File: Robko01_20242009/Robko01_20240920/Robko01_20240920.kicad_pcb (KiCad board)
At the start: 2 copper layers, 178.8 x 143.8 mm, 72 parts, among them J1 Conn_01x04_Pin, J10 Motors, J11 Motors, J12 Conn_01x04_Pin, J13 Conn_01x02_Pin, J14 Conn_01x04_Pin, J15 Conn_01x02_Pin, J16 Conn_01x04_Pin, J17 Conn_01x02_Male, J18 Conn_01x02_Male, J2 Conn_01x02_Pin, J20 Conn_01x02_Male, J21 Conn_01x19_Pin, J22 Conn_01x19_Pin, J23 Conn_01x06_Pin, J24 Conn_01x04_Pin, J25 Conn_01x04_Pin, J26 Conn_01x04_Pin, J27 Conn_01x06_Pin, J28 Conn_01x02_Male, J29 Conn_01x07_Pin, J3 Conn_01x02_Pin, J30 Conn_01x02_Male, J4 Conn_01x04_Pin, J5 Conn_01x02_Pin, J6 Conn_01x04_Pin, J7 Conn_01x02_Male, J8 Conn_01x02_Pin, J9 Motors, K2 G5V-2, SW1 SW_DIP_x04, SW2 SW_DIP_x04, SW3 SW_DIP_x04, SW4 SW_DIP_x04, SW5 SW_DIP_x04, SW7 SW_DIP_x04, U1 LM7805_TO220

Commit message: Add reset button and E-Stop
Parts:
- removed R3: 15k, Resistor_THT:R_Axial_DIN0207_L6.3mm_D2.5mm_P10.16mm_Horizontal
- added J19: Conn_01x02_Male, Connector_PinHeader_2.54mm:PinHeader_1x02_P2.54mm_Vertical, F.Cu at (84.7, 87.9)
- added U2: PC817, Package_DIP:DIP-4_W7.62mm, F.Cu at (127.3, 27.5)
- J20: footprint Connector_PinHeader_2.54mm:PinHeader_1x02_P2.54mm_Vertical -> Connector_PinHeader_2.54mm:PinHeader_1x02_P2.54mm_Horizontal
- R2: value 51k -> 2k
- moved J20 53.5 mm to (101.9, 32.5), turned to -90 degrees
- moved R2 6.05 mm to (139.8, 24.0)
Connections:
- J17 pad 2: unconnected-(J17-Pin_2-Pad2) -> MC_POWER
- J18 pad 1: Net-(J18-Pin_1) -> GND
- J18 pad 2: GND -> Net-(J18-Pin_2)
- J20 pad 2: GND -> MCU_RESET
- J21 pad 2: unconnected-(J21-Pin_2-Pad2) -> MCU_RESET
- R2 pad 2: Net-(J18-Pin_1) -> Net-(R2-Pad2)
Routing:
- net MCU_RESET: track 0.00 -> 69.1 mm, vias 0 -> 2
- net Net-(J18-Pin_1): track 13.7 -> 0.00 mm
- net Net-(J18-Pin_2): track 0.00 -> 7.32 mm
- net MC_POWER: track 310.2 -> 303.8 mm
- net Net-(R2-Pad2): track 0.00 -> 5.60 mm
- net GND: vias 179 -> 178

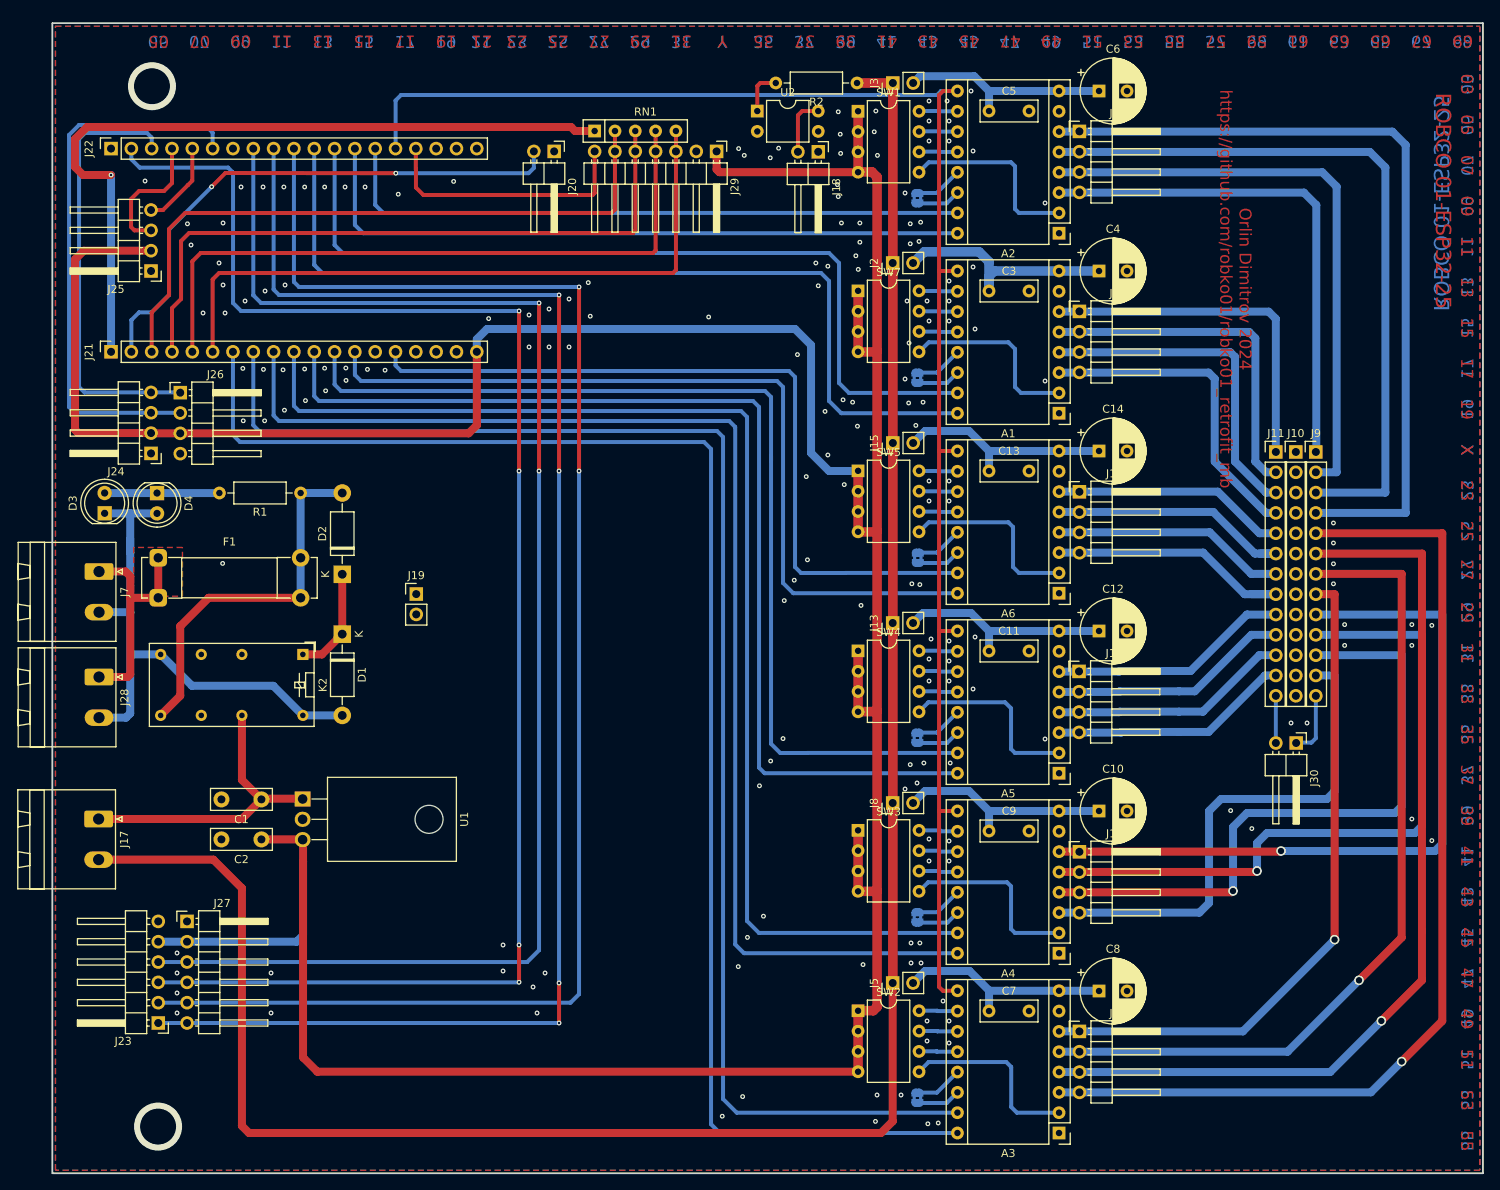
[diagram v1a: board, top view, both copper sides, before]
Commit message: Add UEXT
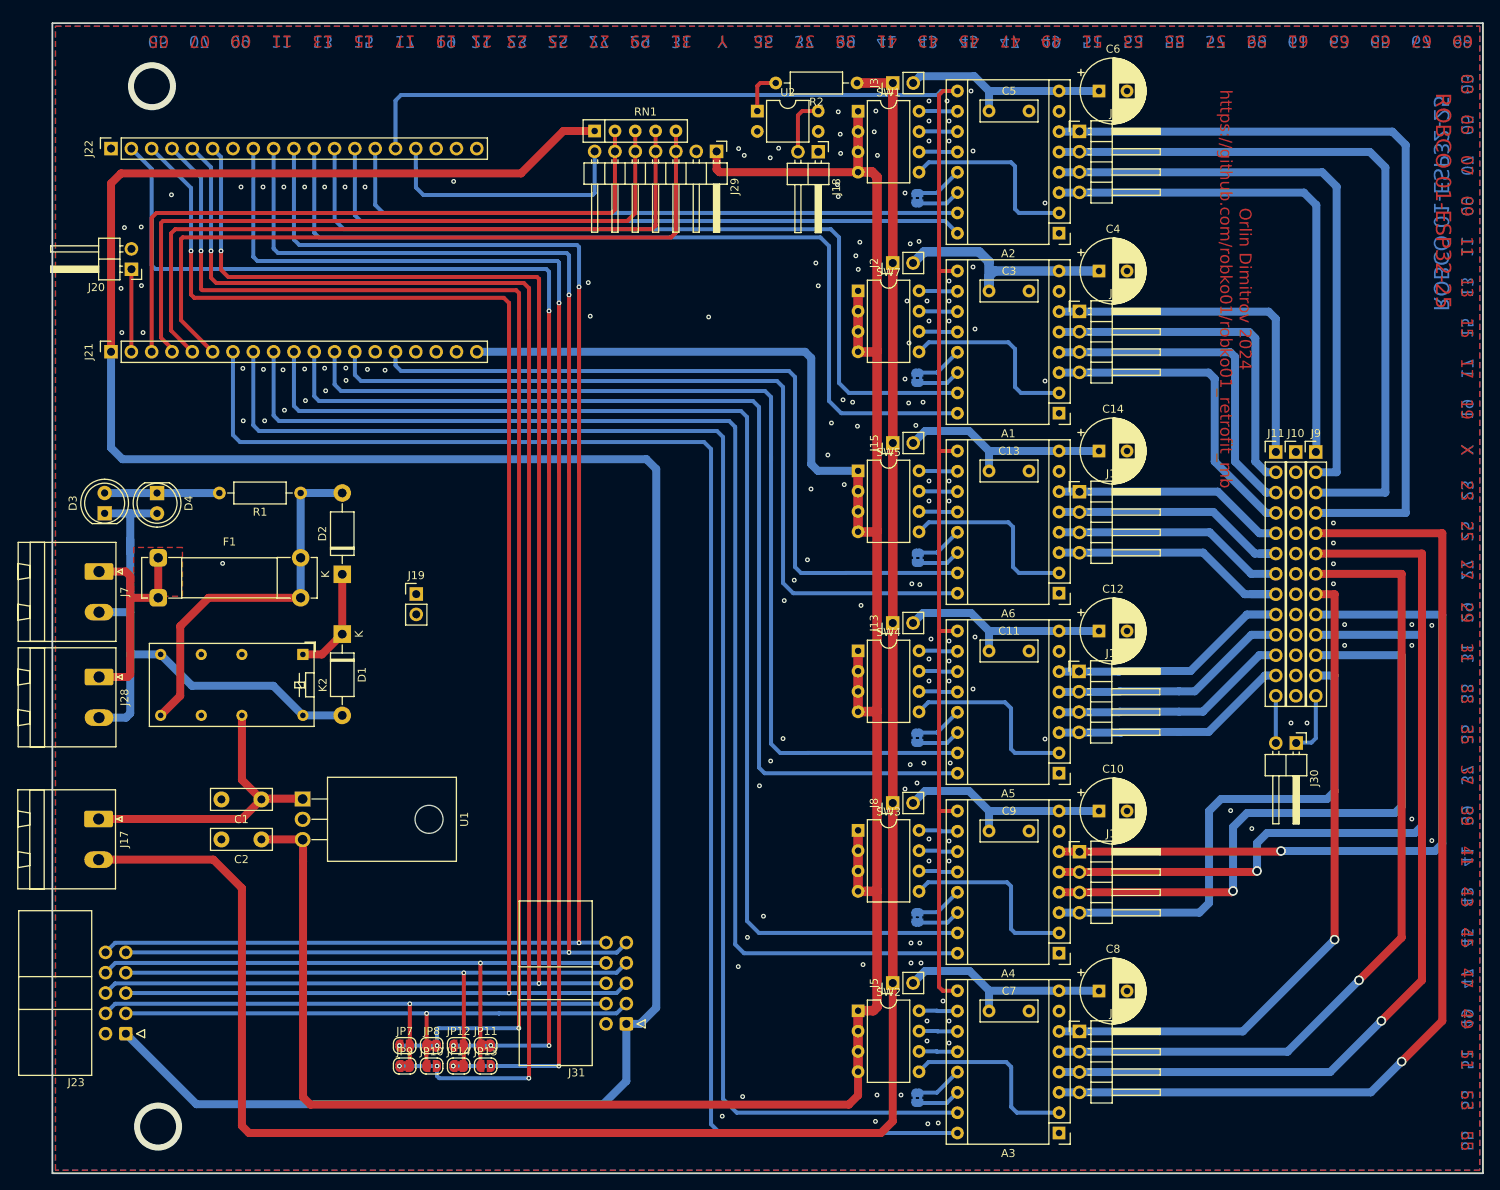
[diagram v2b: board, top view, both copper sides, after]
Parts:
- removed J24, J25, J26: Conn_01x04_Pin, Connector_PinHeader_2.54mm:PinHeader_1x04_P2.54mm_Horizontal
- removed J27: Conn_01x06_Pin, Connector_PinHeader_2.54mm:PinHeader_1x06_P2.54mm_Horizontal
- added J31: Conn_02x05_Odd_Even, Connector_IDC:IDC-Header_2x05_P2.54mm_Horizontal, F.Cu at (110.9, 141.6)
- added JP10: SolderJumper_2_Open, Jumper:SolderJumper-2_P1.3mm_Open_RoundedPad1.0x1.5mm, F.Cu at (86.6, 146.9)
- added JP11: SolderJumper_2_Bridged, Jumper:SolderJumper-2_P1.3mm_Bridged2Bar_RoundedPad1.0x1.5mm, F.Cu at (93.3, 144.3)
- added JP12: SolderJumper_2_Open, Jumper:SolderJumper-2_P1.3mm_Open_RoundedPad1.0x1.5mm, F.Cu at (90.0, 144.3)
- added JP13: SolderJumper_2_Open, Jumper:SolderJumper-2_P1.3mm_Open_RoundedPad1.0x1.5mm, F.Cu at (93.3, 146.9)
- added JP14: SolderJumper_2_Bridged, Jumper:SolderJumper-2_P1.3mm_Bridged2Bar_RoundedPad1.0x1.5mm, F.Cu at (90.0, 146.9)
- added JP7: SolderJumper_2_Open, Jumper:SolderJumper-2_P1.3mm_Open_RoundedPad1.0x1.5mm, F.Cu at (83.2, 144.3)
- added JP8: SolderJumper_2_Bridged, Jumper:SolderJumper-2_P1.3mm_Bridged2Bar_RoundedPad1.0x1.5mm, F.Cu at (86.6, 144.3)
- added JP9: SolderJumper_2_Bridged, Jumper:SolderJumper-2_P1.3mm_Bridged2Bar_RoundedPad1.0x1.5mm, F.Cu at (83.2, 146.9)
- J23: value Conn_01x06_Pin -> Conn_02x05_Odd_Even; footprint Connector_PinHeader_2.54mm:PinHeader_1x06_P2.54mm_Horizontal -> Connector_IDC:IDC-Header_2x05_P2.54mm_Horizontal
- moved J20 54.9 mm to (49.0, 47.3), turned to 180 degrees
- moved J23 4.26 mm to (48.4, 142.8)
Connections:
- J20 pad 1: GND -> MCU_RESET
- J20 pad 2: MCU_RESET -> GND
- J23 pad 1: VSPI_SCK -> +3.3V
- J23 pad 2: VSPI_SS -> GND
- J23 pad 3: VSPI_MOSI -> Net-(J23-Pin_3)
- J23 pad 4: VSPI_MISO -> Net-(J23-Pin_4)
- J23 pad 5: +5V -> SCL
- J23 pad 6: GND -> SDA
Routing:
- net +3.3V: track 96.3 -> 311.9 mm, vias 1 -> 0
- net RX0: track 10.7 -> 178.6 mm, vias 0 -> 4
- net SCL: track 55.0 -> 214.8 mm, vias 0 -> 2
- net TX0: track 16.4 -> 167.9 mm, vias 0 -> 4
- net SDA: track 69.1 -> 211.9 mm, vias 0 -> 2
- net +5V: track 470.9 -> 356.6 mm
- net Net-(J23-Pin_8): track 0.00 -> 76.0 mm, vias 0 -> 1
- net Net-(J23-Pin_7): track 0.00 -> 74.7 mm, vias 0 -> 1
- net Net-(J23-Pin_4): track 0.00 -> 70.9 mm, vias 0 -> 1
- net Net-(J23-Pin_3): track 0.00 -> 69.7 mm, vias 0 -> 1
- net MCU_RESET: track 69.1 -> 10.3 mm, vias 2 -> 0
- net STP_2: track 80.2 -> 115.2 mm
- net VSPI_SS: track 194.0 -> 220.5 mm
- net GPIO35: track 84.9 -> 90.6 mm
- net VSPI_SCK: track 194.7 -> 200.0 mm, vias 4 -> 2
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
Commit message: Change jumpers for UEXT
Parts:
- removed JP10, JP12, JP13: SolderJumper_2_Open, Jumper:SolderJumper-2_P1.3mm_Open_RoundedPad1.0x1.5mm
- removed JP11, JP14, JP9: SolderJumper_2_Bridged, Jumper:SolderJumper-2_P1.3mm_Bridged2Bar_RoundedPad1.0x1.5mm
- added JP15: Jumper_3_Bridged12, Jumper:SolderJumper-3_P1.3mm_Bridged2Bar12_Pad1.0x1.5mm, F.Cu at (85.2, 146.6)
- added JP16: Jumper_3_Bridged12, Jumper:SolderJumper-3_P1.3mm_Bridged2Bar12_Pad1.0x1.5mm, F.Cu at (85.2, 149.1)
- JP7: value SolderJumper_2_Open -> Jumper_3_Bridged12; footprint Jumper:SolderJumper-2_P1.3mm_Open_RoundedPad1.0x1.5mm -> Jumper:SolderJumper-3_P1.3mm_Bridged2Bar12_Pad1.0x1.5mm
- JP8: value SolderJumper_2_Bridged -> Jumper_3_Bridged12; footprint Jumper:SolderJumper-2_P1.3mm_Bridged2Bar_RoundedPad1.0x1.5mm -> Jumper:SolderJumper-3_P1.3mm_Bridged2Bar12_Pad1.0x1.5mm
- moved JP7 8.71 mm to (91.9, 144.8)
- moved JP8 5.72 mm to (91.9, 142.2), turned to 180 degrees
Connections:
- JP7 pad 1: TX0 -> Net-(J23-Pin_7)
- JP7 pad 2: Net-(J23-Pin_4) -> VSPI_MISO
- JP8 pad 1: Net-(J23-Pin_3) -> Net-(J23-Pin_8)
- JP8 pad 2: TX0 -> VSPI_MOSI
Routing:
- net VSPI_MISO: track 186.7 -> 238.4 mm, vias 4 -> 3
- net VSPI_MOSI: track 194.3 -> 243.5 mm, vias 4 -> 3
- net RX0: track 178.6 -> 175.1 mm, vias 4 -> 3
- net Net-(J23-Pin_4): track 70.9 -> 73.1 mm
- net Net-(J23-Pin_3): track 69.7 -> 71.9 mm
- net Net-(J23-Pin_8): track 76.0 -> 73.9 mm
- net Net-(J23-Pin_7): track 74.7 -> 72.6 mm
- net TX0: track 167.9 -> 167.5 mm, vias 4 -> 3

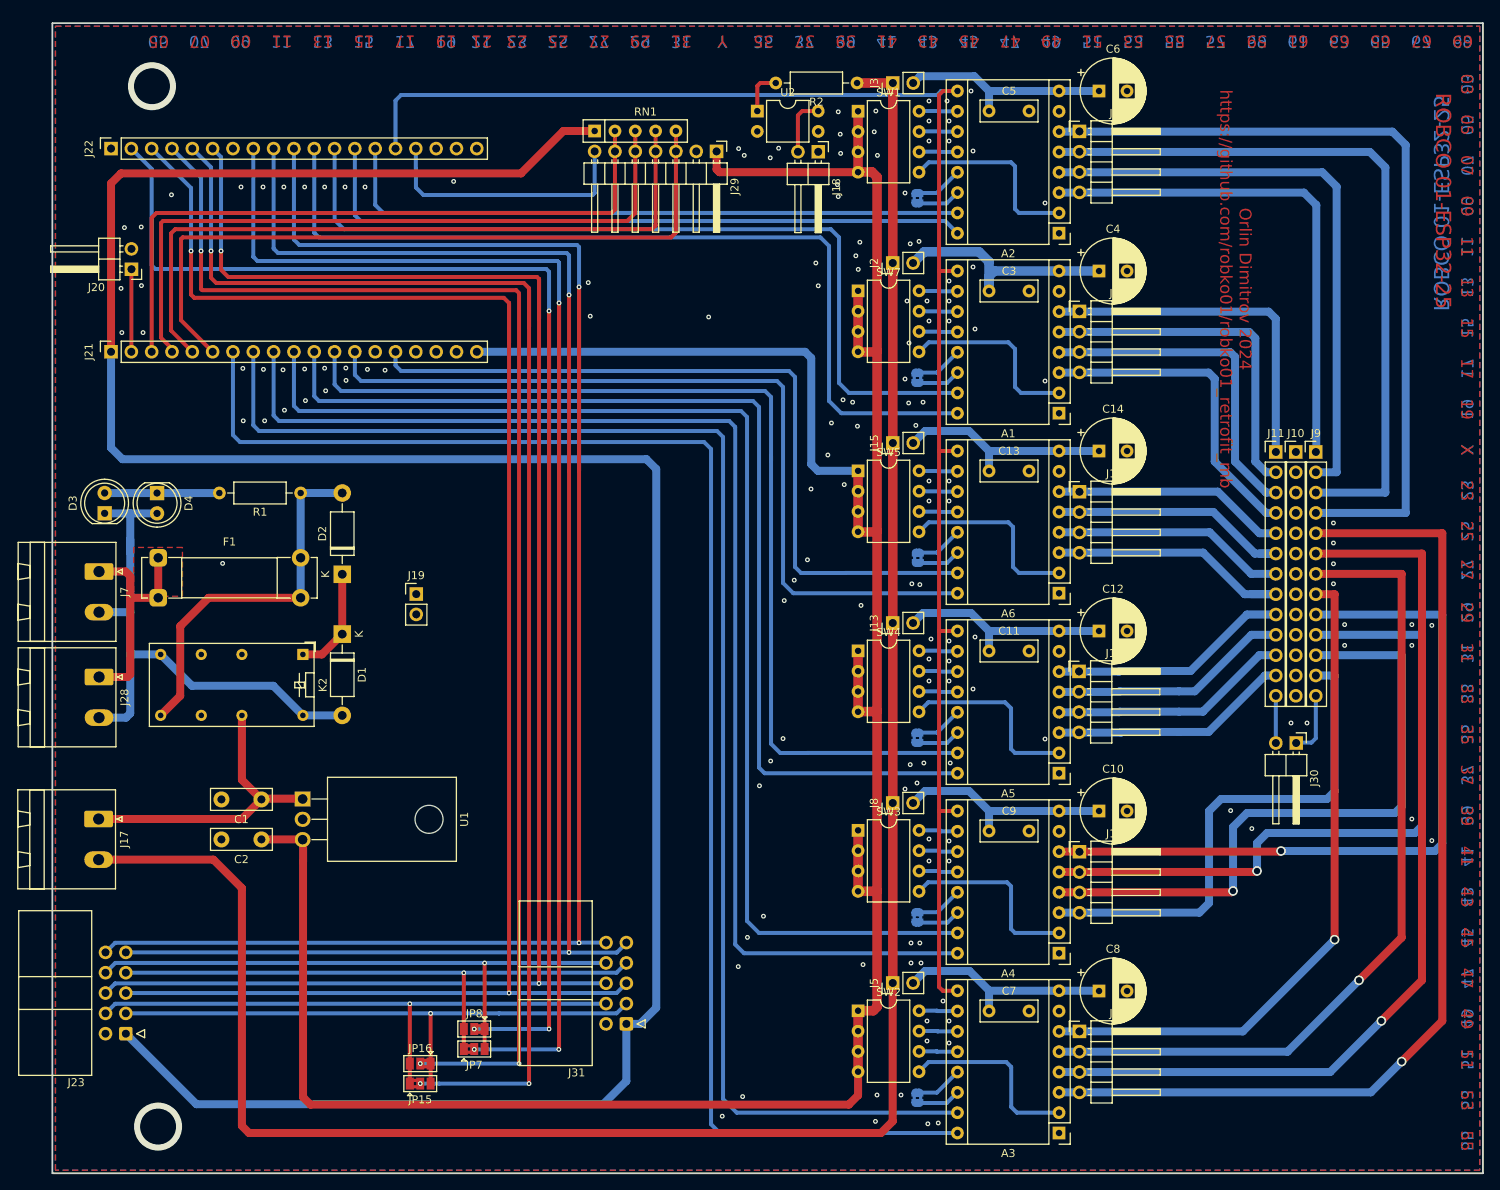
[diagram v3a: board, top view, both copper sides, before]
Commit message: Add USB
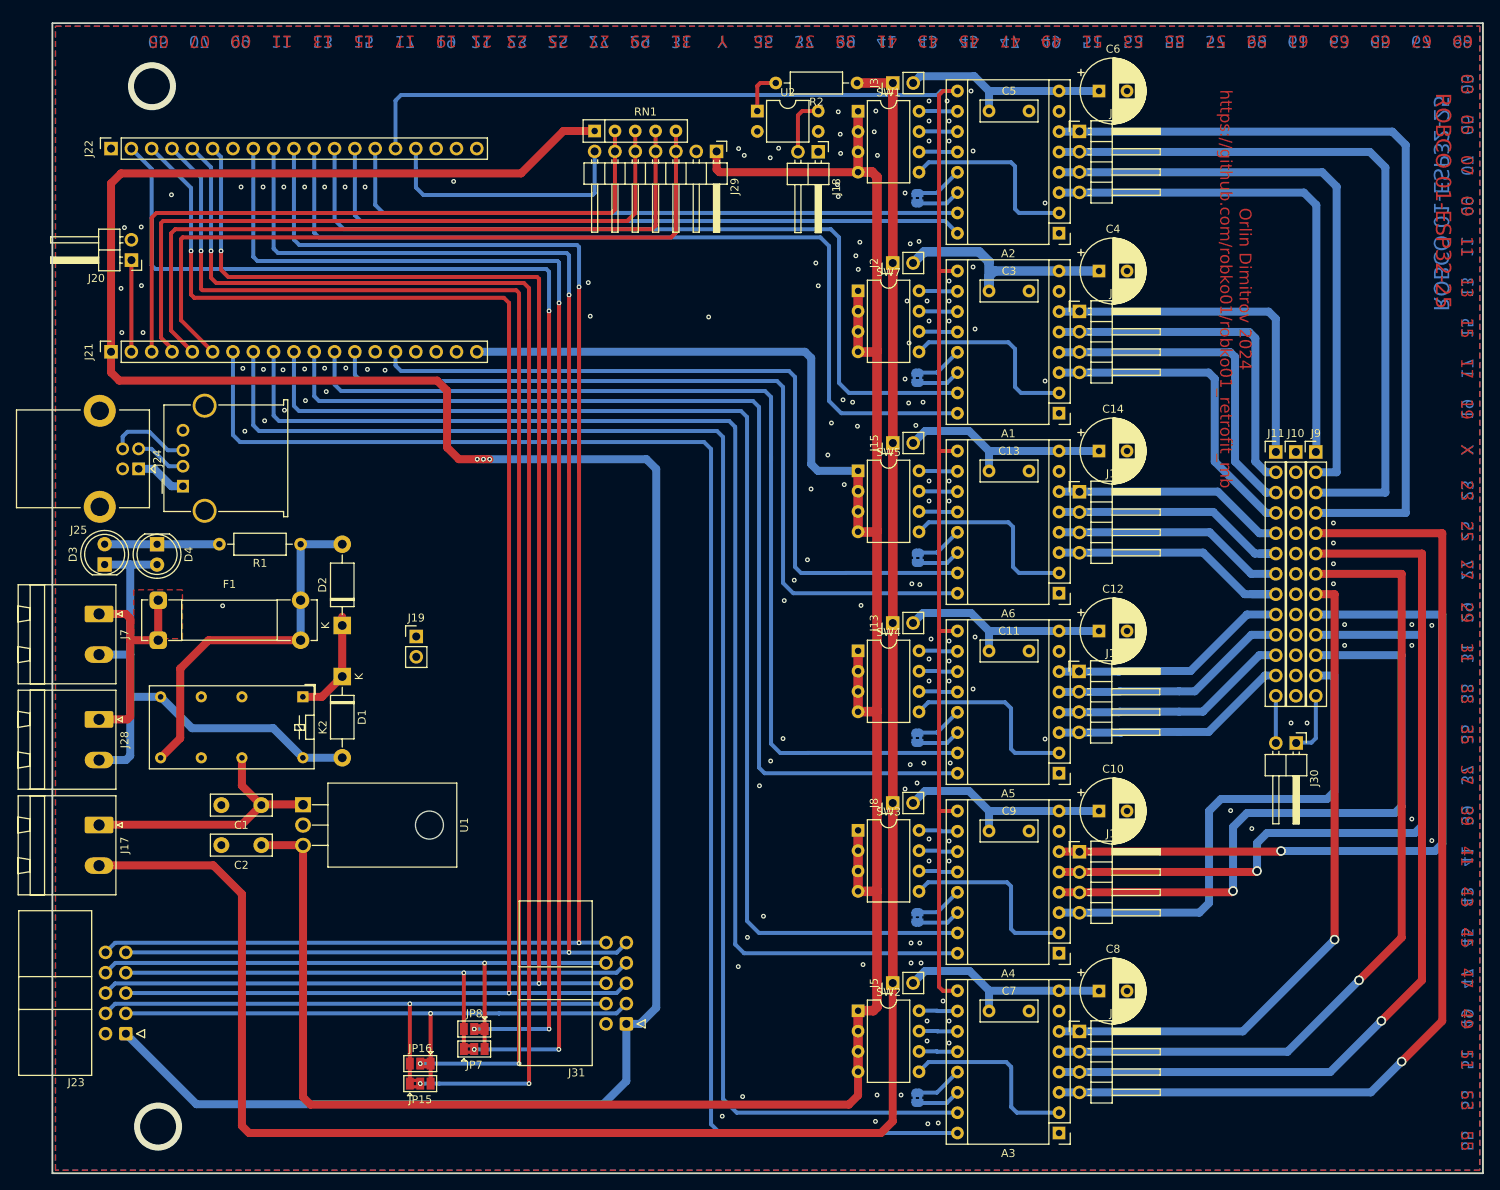
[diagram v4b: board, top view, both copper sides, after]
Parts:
- added J24: USB_A, Connector_USB:USB_A_Molex_67643_Horizontal, F.Cu at (55.5, 74.4)
- added J25: USB_B, Connector_USB:USB_B_Lumberg_2411_02_Horizontal, F.Cu at (50.0, 72.2)
- moved D2 6.40 mm to (75.4, 91.8)
- moved R1 6.40 mm to (70.2, 81.7)
- moved D3 6.40 mm to (45.7, 84.2)
- moved D4 6.40 mm to (52.2, 81.7)
- moved F1 5.30 mm to (52.4, 88.7)
- moved J7 5.30 mm to (45.0, 90.4)
- moved D1 5.30 mm to (75.4, 98.2)
- moved J19 5.30 mm to (84.7, 93.2)
- moved J28 5.30 mm to (45.0, 103.5)
- moved K2 5.30 mm to (70.5, 100.7)
- moved J20 1.13 mm to (49.0, 46.1)
- moved J17 0.75 mm to (45.0, 116.8)
- moved U1 0.72 mm to (70.5, 114.2)
- moved C1 0.72 mm to (65.3, 114.3)
- moved C2 0.72 mm to (65.3, 119.3)
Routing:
- net Net-(J24-D+): track 0.00 -> 10.3 mm
- net Net-(J24-VBUS): track 0.00 -> 6.44 mm
- net Net-(J24-D-): track 0.00 -> 6.44 mm
- net MC_POWER: track 303.8 -> 298.5 mm
- net Net-(D1-A): track 71.0 -> 68.1 mm
- net MCU_RESET: track 10.3 -> 11.5 mm
- net Net-(D2-A): track 47.0 -> 45.9 mm
- net +5V: track 356.6 -> 355.9 mm
- net +3.3V: track 311.9 -> 312.1 mm, vias 0 -> 3
- net GND: vias 149 -> 148
